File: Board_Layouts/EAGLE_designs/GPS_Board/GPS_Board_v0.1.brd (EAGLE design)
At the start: 29 x 46.3 mm, 13 parts

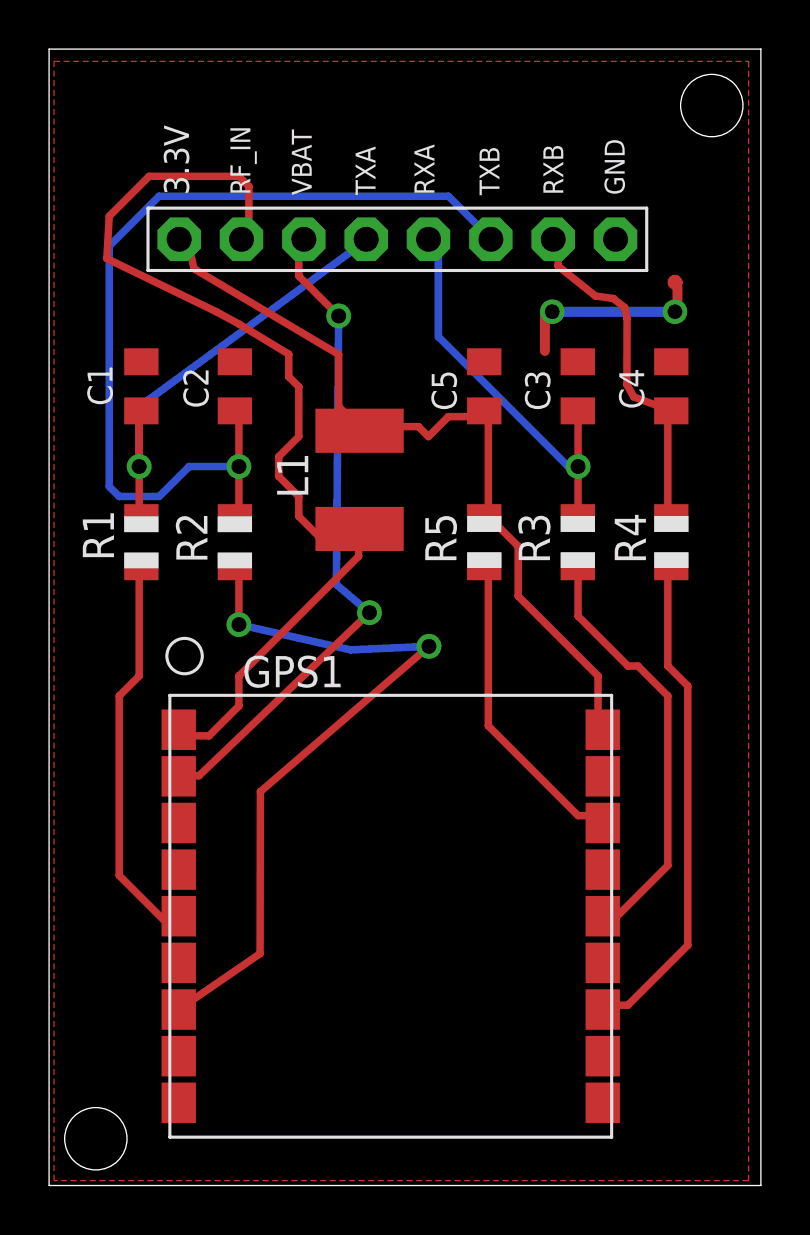
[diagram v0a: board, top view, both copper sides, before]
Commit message: updated GPS Board layout v1.0 ready for production review
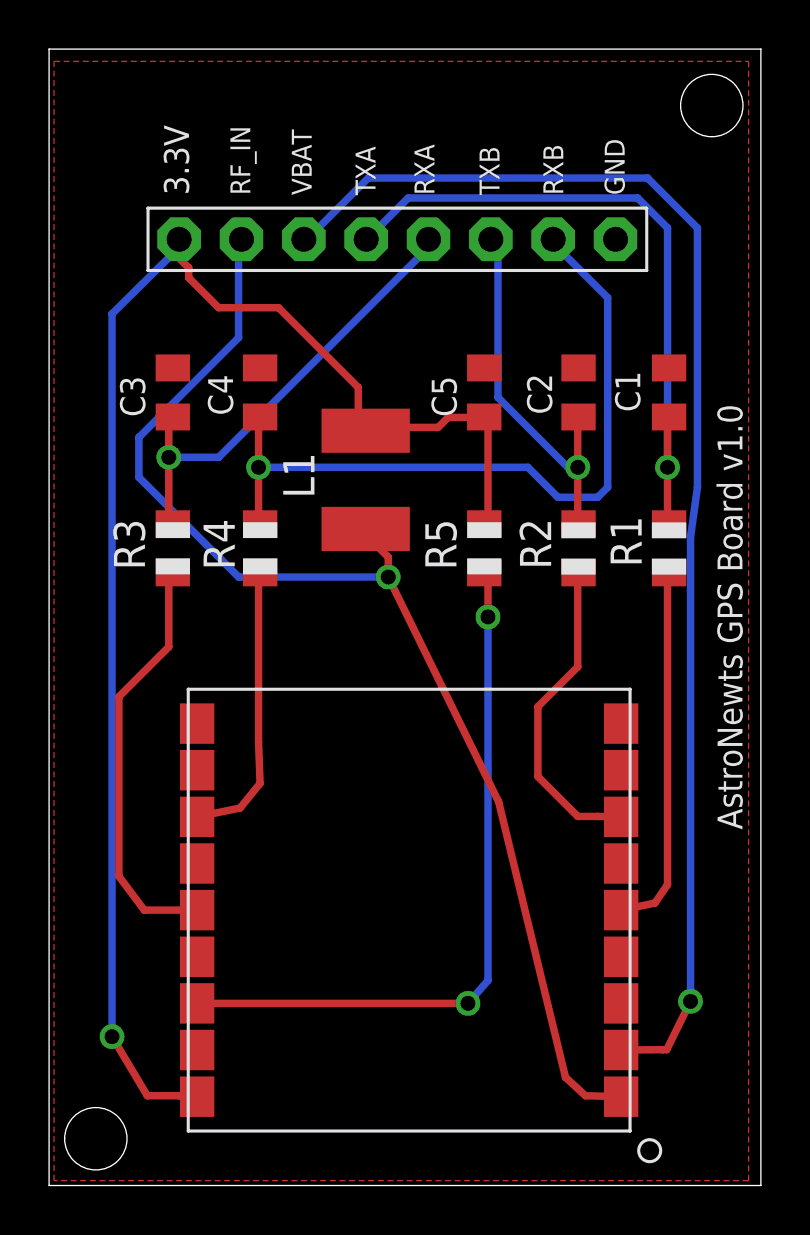
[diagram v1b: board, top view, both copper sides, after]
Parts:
- moved C1 21.5 mm to (25.3, 32.3)
- moved R1 21.5 mm to (25.3, 26.0)
- moved C4 16.8 mm to (8.60, 32.3)
- moved R4 16.8 mm to (8.60, 26.0)
- moved C3 16.5 mm to (5.04, 32.3)
- moved R3 16.5 mm to (5.04, 26.0)
- moved C2 14.0 mm to (21.6, 32.3)
- moved R2 14.0 mm to (21.6, 26.0)
- moved GPS1 0.79 mm to (14.7, 11.2), turned to 180 degrees
- moved C5 0.25 mm to (17.7, 32.3)
- moved L1 0.25 mm to (12.9, 28.8)
- moved R5 0.25 mm to (17.7, 26.0)
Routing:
- net VCC: track 32.6 -> 61.5 mm, vias 0 -> 1
- net VBAT: track 27.0 -> 53.5 mm, vias 2 -> 1
- net TXB: track 37.4 -> 15.3 mm
- net N$2: track 29.9 -> 13.0 mm, vias 2 -> 0
- net RXB: track 14.3 -> 30.7 mm, vias 0 -> 1
- net N$1: track 12.9 -> 28.9 mm, vias 0 -> 2
- net TXA: track 18.4 -> 27.6 mm
- net N$5: track 20.3 -> 11.7 mm
- net GND: track 8.51 -> 0.00 mm
- net RF_IN: track 41.7 -> 49.9 mm, vias 0 -> 1
- net RXA: track 16.4 -> 19.0 mm
- net N$3: track 16.3 -> 15.0 mm
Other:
- board text added: "AstroNewts GPS Board v1.0"
